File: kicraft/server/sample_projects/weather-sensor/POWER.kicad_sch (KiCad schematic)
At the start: 6 parts, among them J1 TYPE-C-31-M-12, U1 3.3V

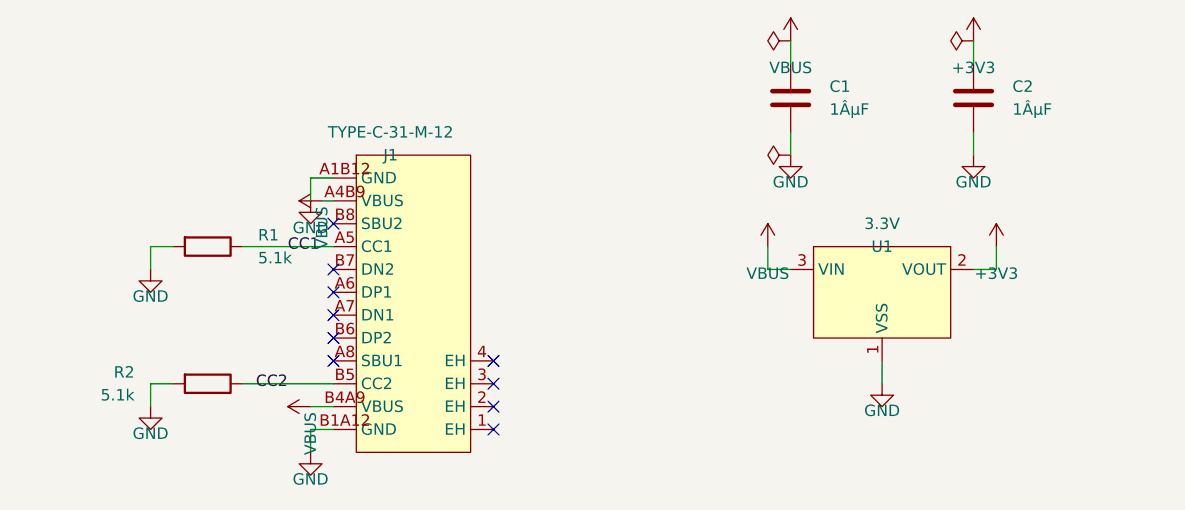
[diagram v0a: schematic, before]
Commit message: feat(showcase): refresh landing samples from self-eval 20260614
Promote the three best boards from self-eval batch 20260614T215540Z
(all grade B) into the landing-page showcase, replacing the regressed
PIR night light (D/45, hit erc_errors + unprogrammable_mcu gates):

- usb-pd-trigger (NEW, featured hero) — 81.0, fab-ready
- weather-sensor (re-promoted; stem A_BMP280_BAROMETRIC -> BMP280_QWIIC_USB_C)
- bench-breakout (re-promoted; 4->5 sheets, 16->19 parts)

Regenerated board.png/hero.png renders and interactive board.glb models
via scripts/promote_to_sample.py. Already live (deploy/restart-web.sh).

Co-Authored-By: Claude Opus 4.8 (1M context) <noreply@anthropic.com>
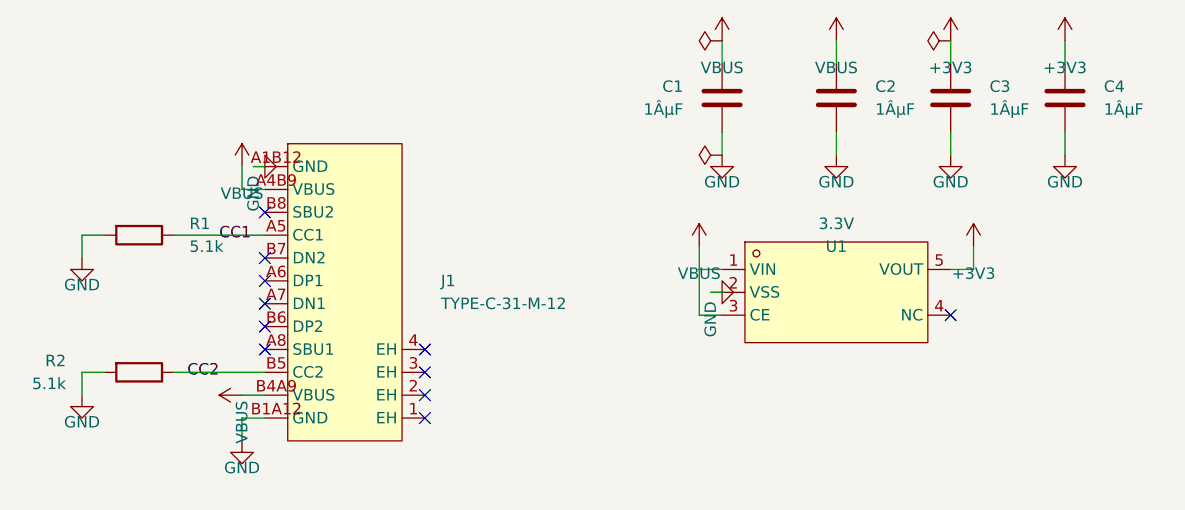
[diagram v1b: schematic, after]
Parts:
- removed U1: 3.3V, xc6206p332mr:SOT-23-3_L2.9-W1.3-P1.90-LS2.4-BR, symbol xc6206p332mr:XC6206P332MR_C5148692
- added C3, C4: 1ÂµF, Capacitor_SMD:C_0805_2012Metric, symbol Device:C
- added U1: 3.3V, me6211c33:SOT-23-5_L3.0-W1.7-P0.95-LS2.8-BL, symbol me6211c33:ME6211C33M5G-N
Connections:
- net +3V3: now also C3.1, C4.1, U1.5 (VOUT); no longer C2.1
- net GND: now also C3.2, C4.2, U1.2 (VSS)
- net VBUS: now also C2.1, U1.1 (VIN), U1.3 (CE)
- no-connect marks 10 -> 11
